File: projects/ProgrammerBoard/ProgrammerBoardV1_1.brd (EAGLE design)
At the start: 34.3 x 31.7 mm, 14 parts, among them J1 EQUISAT-UMBILICAL-CONN, J9 M50-3600542

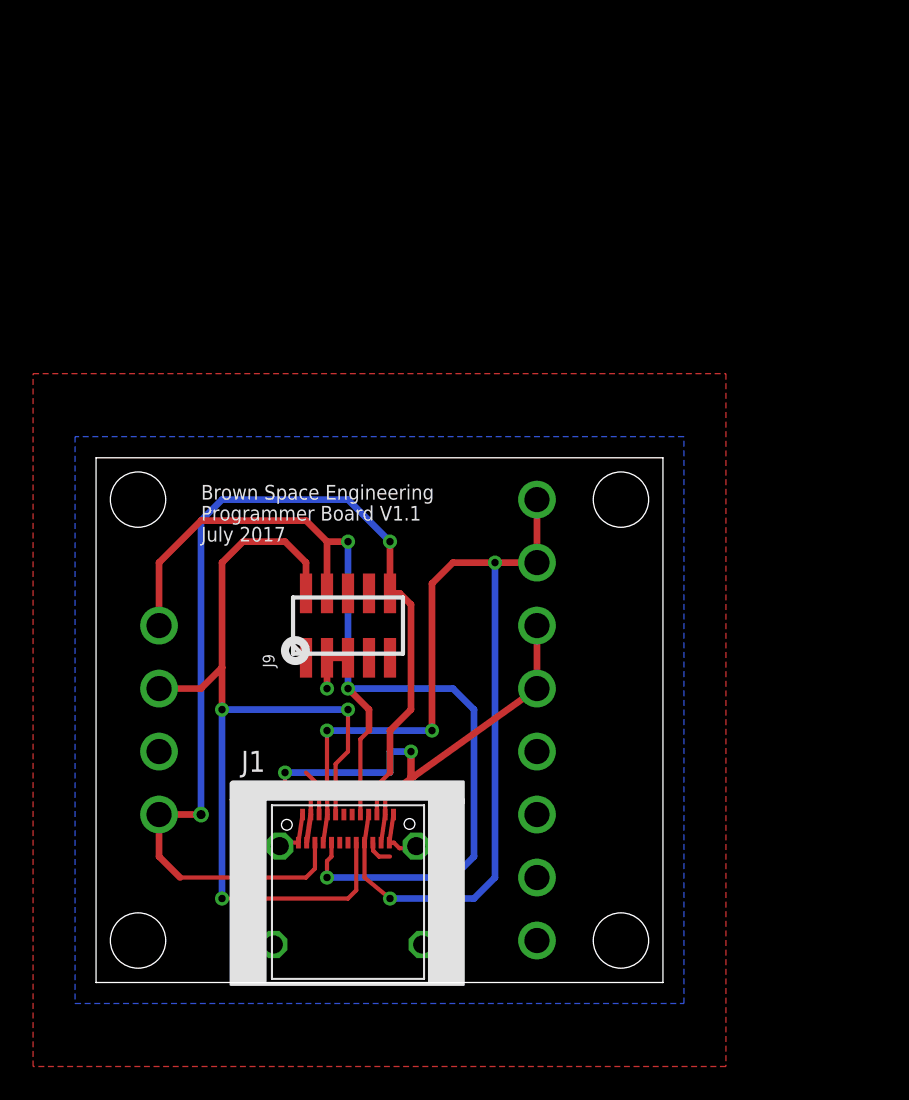
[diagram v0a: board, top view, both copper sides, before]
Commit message: moved connector + rearranged vias
USB connector now as close to edge as possible, vias arranged so
grounds are more spread out and board is more compact
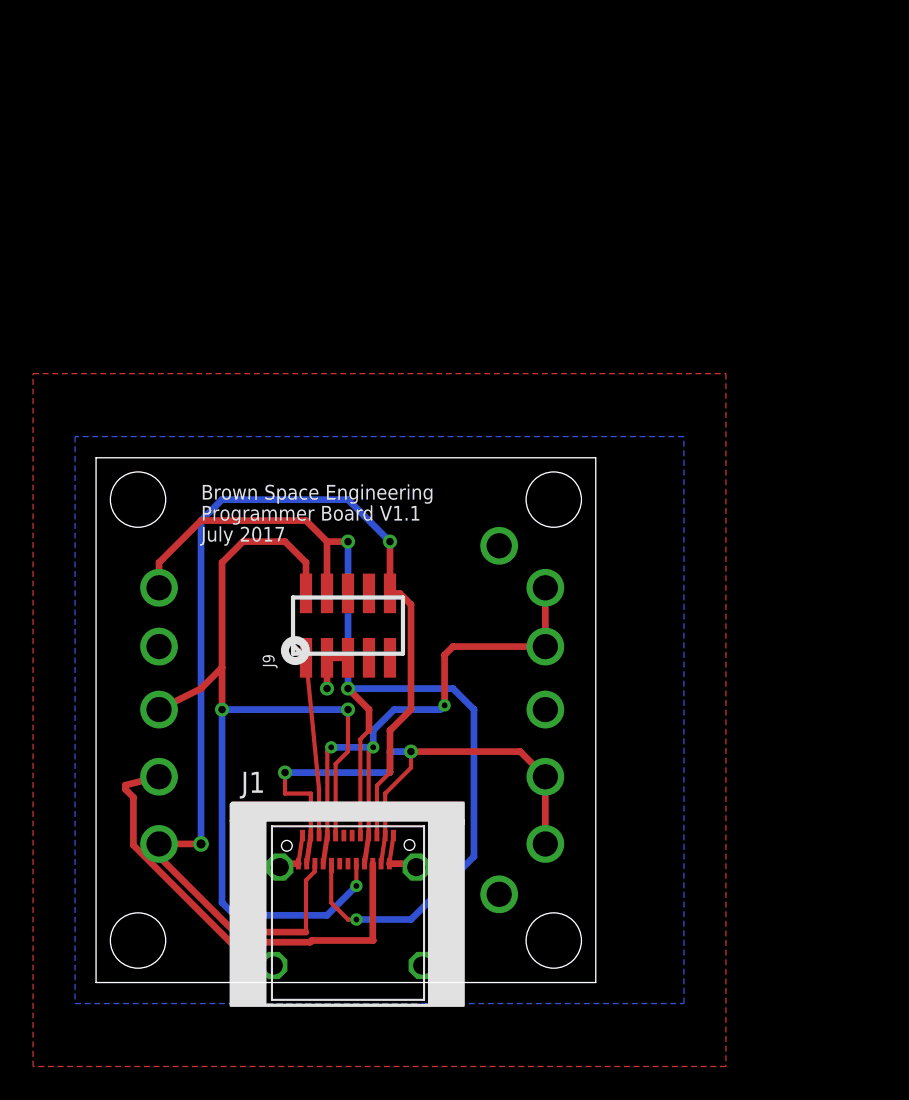
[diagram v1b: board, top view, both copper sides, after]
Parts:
- moved V3 23.7 mm to (3.81, 20.3)
- moved V2 16.4 mm to (24.4, 26.4)
- moved V1 10.2 mm to (27.2, 16.5)
- moved V12 9.41 mm to (27.2, 8.38)
- moved V11 9.16 mm to (27.2, 12.4)
- moved V6 5.36 mm to (27.2, 23.9)
- moved V7 5.11 mm to (27.2, 20.3)
- moved V4 3.61 mm to (24.4, 5.33)
- moved V9 2.29 mm to (3.81, 23.9)
- moved V8 1.78 mm to (3.81, 8.38)
- moved V10 1.52 mm to (3.81, 12.4)
- moved J1 1.27 mm to (15.2, 8.89)
- moved V5 1.27 mm to (3.81, 16.5)
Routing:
- net 3V3: track 4.53 -> 38.4 mm
- net UMB-CHG: track 64.5 -> 35.7 mm, vias 4 -> 3
- net RESETN: track 65.9 -> 70.5 mm
- net SWDIO: track 58.1 -> 59.3 mm
- net SWCLK: track 65.9 -> 66.6 mm
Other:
- board size 34.3 x 31.7 mm -> 30.2 x 31.7 mm

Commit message: Updates to programmer board with correct connector, addition of TVS diodes, modified layout, and updated silkscreen.
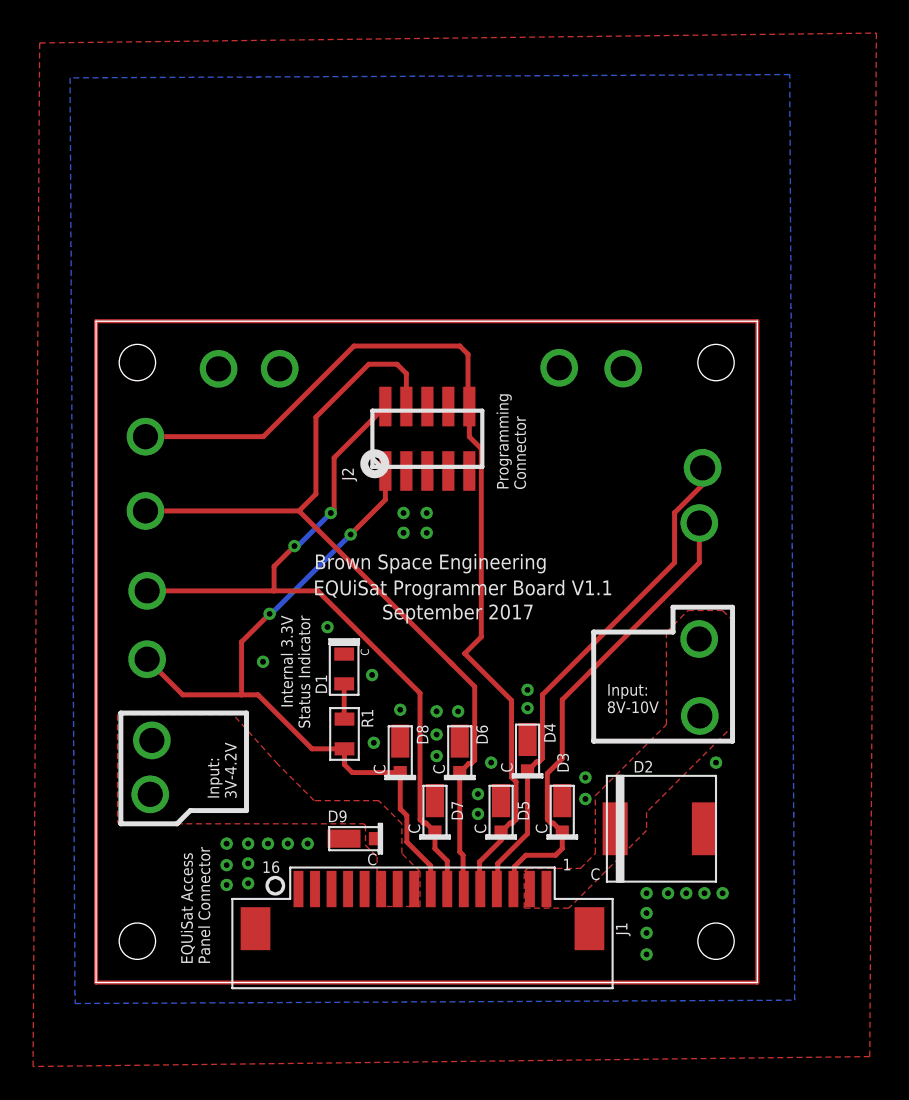
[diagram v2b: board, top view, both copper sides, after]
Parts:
- removed J9: M50-3600542, BrownSpaceEngineering:10PINMALE
- added D1: LED0805, BrownSpaceEngineering:0805-D
- added D2: SMCJ11A, BrownSpaceEngineering:DO-214AB
- added D3, D4, D5, D6, D7, D8, D9: MSP5.0A, BrownSpaceEngineering:MICROSMP
- added J2: M50-3600542, BrownSpaceEngineering:10PINMALE
- added MTG1, MTG2, MTG3, MTG4: (no value), BrownSpaceEngineering:M2-NPTH
- added R1: 150R, BrownSpaceEngineering:0805
- added V13: USART-RX, BrownSpaceEngineering:VIA-60MIL
- added V14: USART-TX, BrownSpaceEngineering:VIA-60MIL
- J1: value EQUISAT-UMBILICAL-CONN -> FFC-16REVERSE; device BrownSpaceEngineering:USB-C-RCPT-SMT -> BrownSpaceEngineering:68611614422-REVERSE
- moved V4 32.7 mm to (31.9, 37.1)
- moved V1 26.1 mm to (11.1, 37.1), turned to 270 degrees
- moved V8 24.6 mm to (2.99, 33.0), turned to 180 degrees
- moved V12 24.1 mm to (3.28, 11.4)
- moved V11 23.9 mm to (3.38, 14.6)
- moved V3 17.2 mm to (7.41, 37.1)
- moved V6 12.1 mm to (36.5, 16.1), turned to 180 degrees
- moved V2 11.4 mm to (28.0, 37.2), turned to 180 degrees
- moved V7 9.31 mm to (36.5, 20.8), turned to 90 degrees
- moved V5 7.22 mm to (3.09, 23.7), turned to 180 degrees
- moved V10 7.14 mm to (3.09, 19.6), turned to 180 degrees
- moved V9 4.72 mm to (2.99, 28.5), turned to 180 degrees
- moved J1 4.41 mm to (12.2, 5.66)
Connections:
- removed net SWCLK: J1.A8, J1.B8, J9.P9, V9.P$1
- new net N$2: D1.A, R1.1
- new net SWDCLK: D6.C, J1.P6, J2.P9, V9.P$1
- new net USART-RX: D4.C, J1.P4, V13.P$1
- new net USART-TX: D3.C, J1.P3, V14.P$1
- net 3V3: now also D8.C, J1.P8, J2.P1, R1.2; no longer J1.A3, J1.B3, J9.P1
- net GND: now also D1.C, D2.A, D3.A, D4.A, D5.A, D6.A, D7.A, D8.A, D9.A, J1.P$17, J1.P$18, J1.P12, J1.P13, J1.P14, J1.P15, J1.P16, J2.P2, J2.P3; no longer J1.A1, J1.A12, J1.B1, J1.B12, J1.GND@1, J1.GND@2, J1.GND@3, J1.GND@4, J9.P2, J9.P3
- net RESETN: now also D5.C, J1.P5, J2.P6; no longer J1.A10, J1.B10, J9.P6
- net SWDIO: now also D7.C, J1.P7, J2.P10; no longer J1.A5, J1.B5, J9.P10
- net UMB-CHG: now also D2.C, J1.P1, J1.P2; no longer J1.A4, J1.A9, J1.B4, J1.B9
- net VIN-EXT: now also D9.C, J1.P10, J1.P11, J1.P9; no longer J1.A11, J1.A2, J1.B11, J1.B2
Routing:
- net N$1: track 0.00 -> 160.0 mm
- net SWCLK: track 66.6 -> 0.00 mm, vias 3 -> 0
- net SWDCLK: track 0.00 -> 52.5 mm
- net VIN-EXT: track 36.2 -> 0.00 mm, vias 2 -> 0
- net UMB-CHG: track 35.7 -> 0.00 mm, vias 3 -> 0
- net USART-RX: track 0.00 -> 30.7 mm
- net USART-TX: track 0.00 -> 28.8 mm
- net SWDIO: track 59.3 -> 45.7 mm, vias 3 -> 2
- net RESETN: track 70.5 -> 57.4 mm, vias 2 -> 0
- net GND: track 9.50 -> 0.00 mm, vias 1 -> 38
- net 3V3: track 38.4 -> 43.8 mm, vias 0 -> 2
- net N$2: track 0.00 -> 2.14 mm
- added copper zone on layer 1, net GND
- added copper zone on layer 1, net UMB-CHG
- added copper zone on layer 1, net VIN-EXT
- removed copper zone on layer 1, net 3V3
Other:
- board size 30.2 x 31.7 mm -> 40 x 40 mm
- board text added: "EQUiSat Access Panel Connector"
- board text added: "EQUiSat Programmer Board V1.1"
- board text added: "Input: 3V-4.2V"
- board text added: "Input: 8V-10V"
- board text added: "Internal 3.3V Status Indicator"
- board text added: "Programming Connector"
- board text added: "September 2017"
- board text removed: "July 2017"
- board text removed: "Programmer Board V1.1"

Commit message: Finished programmer board and added output files to repo. Addiong of LDOs and continued fixes and updates to battery board v2.
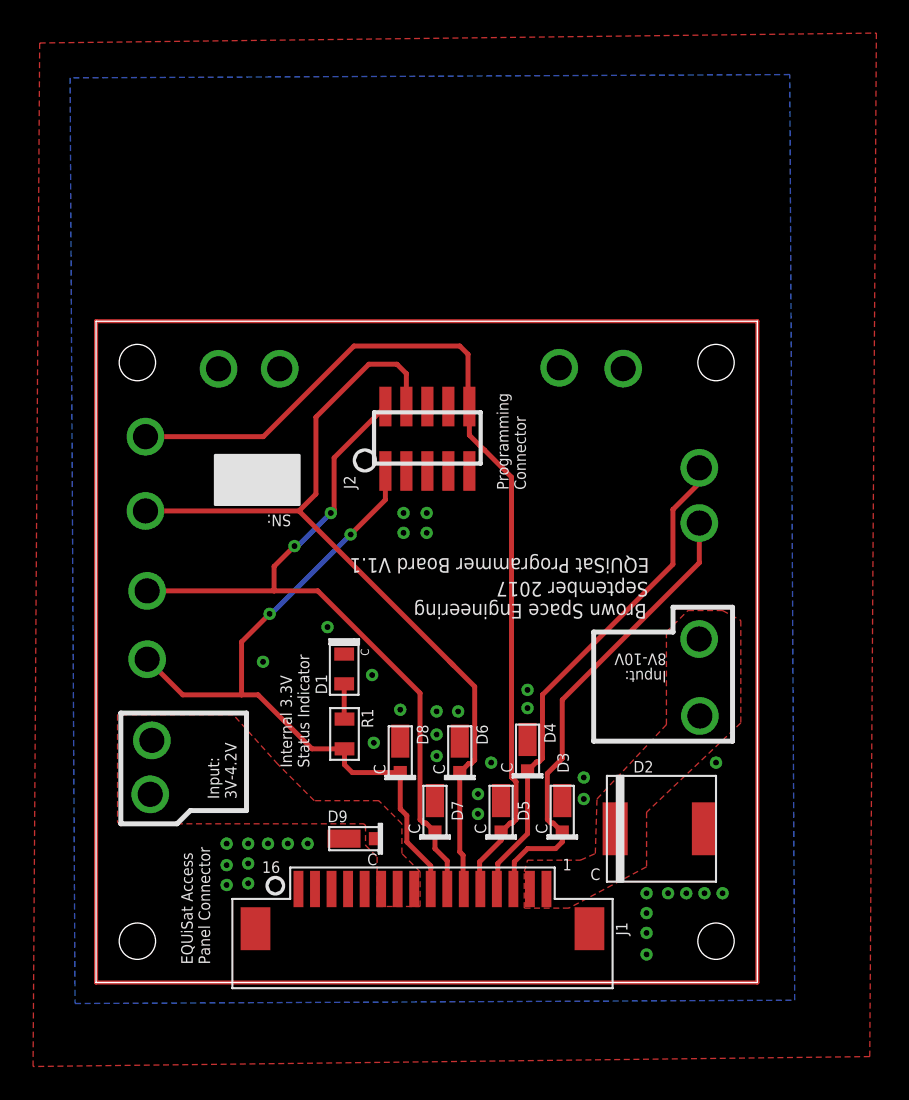
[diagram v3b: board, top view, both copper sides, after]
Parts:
- moved V13 0.20 mm to (36.5, 31.1)
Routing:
- net RESETN: track 57.4 -> 56.6 mm
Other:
- board text added: "SN:"
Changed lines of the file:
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@@
 <wire x1="40" y1="40" x2="0" y2="40" width="0" layer="20"/>
 <wire x1="0" y1="40" x2="0" y2="0" width="0" layer="20"/>
-<text x="13.196" y="24.998" size="0.889" layer="25">Brown Space Engineering</text>
-<text x="13.142" y="23.428" size="0.889" layer="25">EQUiSat Programmer Board V1.1</text>
-<text x="17.296" y="21.966" size="0.889" layer="25">September 2017</text>
+<text x="33.304" y="22.902" size="0.889" layer="25" rot="SR180">Brown Space Engineering</text>
+<text x="33.458" y="25.672" size="0.889" layer="25" rot="SR180">EQUiSat Programmer Board V1.1</text>
+<text x="33.404" y="24.234" size="0.889" layer="25" rot="SR180">September 2017</text>
 <text x="26" y="29.8" size="0.7" layer="25" rot="R90">Programming
 Connector</text>
@@
 <text x="8.5" y="11.1" size="0.7" layer="25" rot="R90">Input:
 3V-4.2V</text>
-<text x="30.9" y="16.3" size="0.7" layer="25">Input:
+<text x="34.5" y="19.9" size="0.7" layer="25" rot="SR180">Input:
 8V-10V</text>
 <wire x1="1.5" y1="16.3" x2="1.5" y2="9.6" width="0.3" layer="25"/>
@@
 <wire x1="34.9" y1="21.2" x2="30.1" y2="21.2" width="0.3" layer="25"/>
 <wire x1="30.1" y1="21.2" x2="30.1" y2="14.6" width="0.3" layer="25"/>
-<text x="11.2" y="22.2" size="0.7" layer="25" rot="R270">Internal 3.3V
+<text x="12.9" y="13" size="0.7" layer="25" rot="R90">Internal 3.3V
 Status Indicator</text>
+<text x="11.8" y="28.3" size="0.7" layer="21" rot="SR180">SN:</text>
+<polygon width="0.1524" layer="21">
+<vertex x="7.2" y="31.9"/>
+<vertex x="7.2" y="28.9"/>
+<vertex x="12.3" y="28.9"/>
+<vertex x="12.3" y="31.9"/>
+</polygon>
 </plain>
 <attributes>
@@
 <elements>
 <element name="J2" library="BrownSpaceEngineering" package="10PINMALE" value="M50-3600542" x="20.04" y="32.89" smashed="yes">
-<attribute name="NAME" x="15.595" y="30.35" size="0.7112" layer="21" rot="R90"/>
+<attribute name="NAME" x="15.695" y="29.85" size="0.7112" layer="21" rot="R90"/>
 </element>
 <element name="V1" library="BrownSpaceEngineering" package="VIA-60MIL" value="GND" x="11.11" y="37.122" smashed="yes" rot="R270">
@@
 </element>
 <element name="V6" library="BrownSpaceEngineering" package="VIA-60MIL" value="UMB-CHG" x="36.522" y="16.124" smashed="yes" rot="R180">
-<attribute name="VALUE" x="30.958" y="18.536" size="0.762" layer="27"/>
+<attribute name="VALUE" x="35.342" y="17.764" size="0.762" layer="27" rot="SR180"/>
 </element>
 <element name="V7" library="BrownSpaceEngineering" package="VIA-60MIL" value="UMB-CHG" x="36.48" y="20.778" smashed="yes" rot="R90"/>
@@
 <attribute name="NAME" x="32.144" y="2.844" size="0.7" layer="21" rot="R90"/>
 </element>
-<element name="V13" library="BrownSpaceEngineering" package="VIA-60MIL" value="USART-RX" x="36.69" y="31.132" smashed="yes" rot="R180">
-<attribute name="VALUE" x="34.16" y="31.262" size="0.762" layer="27" rot="R180"/>
+<element name="V13" library="BrownSpaceEngineering" package="VIA-60MIL" value="USART-RX" x="36.49" y="31.132" smashed="yes" rot="R180">
+<attribute name="VALUE" x="33.66" y="31.162" size="0.762" layer="27" rot="SR180"/>
 </element>
 <element name="V14" library="BrownSpaceEngineering" package="VIA-60MIL" value="USART-TX" x="36.49" y="27.792" smashed="yes" rot="R180">
-<attribute name="VALUE" x="34.16" y="27.922" size="0.762" layer="27" rot="R180"/>
+<attribute name="VALUE" x="33.86" y="28.122" size="0.762" layer="27" rot="SR180"/>
 </element>
 <element name="D1" library="BrownSpaceEngineering" package="0805-D" value="LED0805" x="15.008" y="18.966" rot="R90"/>
@@
 <via x="21.9" y="16.4" extent="1-16" drill="0.35"/>
 <via x="26.1" y="16.6" extent="1-16" drill="0.35"/>
-<via x="29.6" y="11.1" extent="1-16" drill="0.35"/>
+<via x="29.5" y="11.1" extent="1-16" drill="0.35"/>
 <via x="20.6" y="15" extent="1-16" drill="0.35"/>
 <via x="20.6" y="16.4" extent="1-16" drill="0.35"/>
@@
 <via x="23.1" y="11.4" extent="1-16" drill="0.35"/>
 <via x="26.1" y="17.7" extent="1-16" drill="0.35"/>
-<via x="29.6" y="12.4" extent="1-16" drill="0.35"/>
+<via x="29.5" y="12.4" extent="1-16" drill="0.35"/>
 <via x="16.8" y="14.5" extent="1-16" drill="0.35"/>
 <via x="14" y="21.5" extent="1-16" drill="0.35"/>
@@
 <wire x1="24.5" y1="9.1" x2="25.0468" y2="9.6468" width="0.3" layer="1"/>
 <wire x1="25.0468" y1="9.6468" x2="25.1963" y2="9.6468" width="0.3" layer="1"/>
-<wire x1="25.1314" y1="17.0686" x2="22.3" y2="19.9" width="0.3" layer="1"/>
+<wire x1="25.1314" y1="30.5686" x2="24.6" y2="31.1" width="0.3" layer="1"/>
 <wire x1="25.4032" y1="12.1463" x2="25.1314" y2="12.4181" width="0.3" layer="1"/>
-<wire x1="25.1314" y1="12.4181" x2="25.1314" y2="17.0686" width="0.3" layer="1"/>
-<wire x1="22.58" y1="33.0095" x2="22.58" y2="34.84" width="0.3" layer="1"/>
-<wire x1="23.3032" y1="32.2863" x2="22.58" y2="33.0095" width="0.3" layer="1"/>
-<wire x1="22.3" y1="19.9" x2="23.3032" y2="20.9032" width="0.3" layer="1"/>
-<wire x1="23.3032" y1="20.9032" x2="23.3032" y2="32.2863" width="0.3" layer="1"/>
+<wire x1="25.1314" y1="12.4181" x2="25.1314" y2="30.5686" width="0.3" layer="1"/>
+<wire x1="22.58" y1="33.1095" x2="22.58" y2="34.84" width="0.3" layer="1"/>
+<wire x1="23.2032" y1="32.4863" x2="22.58" y2="33.1095" width="0.3" layer="1"/>
+<wire x1="24.6" y1="31.1" x2="23.5032" y2="32.2032" width="0.3" layer="1"/>
+<wire x1="23.5032" y1="32.2032" x2="23.2032" y2="32.4863" width="0.3" layer="1"/>
 <wire x1="22.58" y1="34.84" x2="22.5" y2="34.92" width="0.3" layer="1"/>
 <wire x1="22.5" y1="34.92" x2="22.5" y2="38" width="0.3" layer="1"/>
@@
 <polygon width="0.1524" layer="1">
 <vertex x="25.9" y="6.7"/>
-<vertex x="26.1" y="6.9"/>
-<vertex x="29.3" y="6.9"/>
+<vertex x="26.1" y="7.4"/>
+<vertex x="29.3" y="7.4"/>
 <vertex x="30.2" y="7.8"/>
-<vertex x="30.2" y="11.3"/>
+<vertex x="30.3" y="11.1"/>
 <vertex x="34.5" y="15.6"/>
 <vertex x="34.5" y="21.2"/>
 <vertex x="35.8" y="22.5"/>
 <vertex x="37.9" y="22.5"/>
-<vertex x="38.6" y="21.8"/>
-<vertex x="38.6" y="15.6"/>
+<vertex x="39" y="21.9"/>
+<vertex x="39" y="15.7"/>
 <vertex x="33.3" y="10.3"/>
-<vertex x="33.3" y="9.2"/>
+<vertex x="33.3" y="7"/>
 <vertex x="28.6" y="4.5"/>
 <vertex x="25.9" y="4.5"/>
@@
 <contactref element="D3" pad="C"/>
 <wire x1="25.244" y1="5.656" x2="25.3" y2="5.712" width="0.3" layer="1"/>
-<wire x1="25.3" y1="5.712" x2="25.3" y2="7" width="0.3" layer="1"/>
-<wire x1="25.3" y1="7" x2="26" y2="7.7" width="0.3" layer="1"/>
-<wire x1="26" y1="7.7" x2="27.8" y2="7.7" width="0.3" layer="1"/>
-<wire x1="27.8" y1="7.7" x2="28.2" y2="8.1" width="0.3" layer="1"/>
-<wire x1="28.2" y1="8.1" x2="28.2" y2="9.1" width="0.3" layer="1"/>
+<wire x1="25.3" y1="5.712" x2="25.3" y2="7.3" width="0.3" layer="1"/>
+<wire x1="25.3" y1="7.3" x2="26.1" y2="8.1" width="0.3" layer="1"/>
+<wire x1="26.1" y1="8.1" x2="27.8" y2="8.1" width="0.3" layer="1"/>
+<wire x1="27.8" y1="8.1" x2="28.2" y2="8.5" width="0.3" layer="1"/>
+<wire x1="28.2" y1="8.5" x2="28.2" y2="9.1" width="0.3" layer="1"/>
 <wire x1="27.5037" y1="9.6468" x2="27.2968" y2="9.8537" width="0.3" layer="1"/>
 <wire x1="27.2968" y1="9.8537" x2="27.2968" y2="12.6463" width="0.3" layer="1"/>
-<wire x1="28.2" y1="17.1" x2="29.9" y2="18.8" width="0.3" layer="1"/>
-<wire x1="29.9" y1="18.8" x2="30" y2="18.9" width="0.3" layer="1"/>
 <wire x1="28.2" y1="9.1" x2="27.6532" y2="9.6468" width="0.3" layer="1"/>
 <wire x1="27.6532" y1="9.6468" x2="27.5037" y2="9.6468" width="0.3" layer="1"/>
 <wire x1="28.2" y1="13.5495" x2="28.2" y2="17.1" width="0.3" layer="1"/>
 <wire x1="27.2968" y1="12.6463" x2="28.2" y2="13.5495" width="0.3" layer="1"/>
-<wire x1="29.9" y1="18.8" x2="36.49" y2="25.39" width="0.3" layer="1"/>
+<wire x1="28.2" y1="17.1" x2="36.49" y2="25.39" width="0.3" layer="1"/>
 <wire x1="36.49" y1="25.39" x2="36.49" y2="27.792" width="0.3" layer="1"/>
 </signal>
@@
 <wire x1="26.6468" y1="13.3468" x2="26.7963" y2="13.3468" width="0.3" layer="1"/>
 <wire x1="27.0032" y1="13.5537" x2="27.0032" y2="17.4032" width="0.3" layer="1"/>
-<wire x1="36.69" y1="30.10795" x2="36.69" y2="31.132" width="0.3" layer="1"/>
-<wire x1="34.9938" y1="25.3938" x2="34.9938" y2="28.41175" width="0.3" layer="1"/>
-<wire x1="34.9938" y1="28.41175" x2="36.69" y2="30.10795" width="0.3" layer="1"/>
-<wire x1="27.0032" y1="17.4032" x2="34.9938" y2="25.3938" width="0.3" layer="1"/>
+<wire x1="36.49" y1="30.20795" x2="36.49" y2="31.132" width="0.3" layer="1"/>
+<wire x1="34.8938" y1="25.2938" x2="34.8938" y2="28.61175" width="0.3" layer="1"/>
+<wire x1="34.8938" y1="28.61175" x2="36.49" y2="30.20795" width="0.3" layer="1"/>
+<wire x1="27.0032" y1="17.4032" x2="34.8938" y2="25.2938" width="0.3" layer="1"/>
 </signal>
 <signal name="SWDCLK">
